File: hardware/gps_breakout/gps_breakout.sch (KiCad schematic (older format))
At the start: 33 parts

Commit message: started layout of gps board
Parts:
- C1, C10, C11, C12, C13, C2, C3, C4, C5, C6, C7, C8, C9: renamed from C?; footprint (none) -> Capacitors_SMD:C_0603
- CON1: renamed from CON?; footprint (none) -> Connect:USB_Mini-B
- D1, D2, D3: renamed from D?; footprint (none) -> LEDs:LED-0603
- L1, L2, L3, L4: renamed from L?; footprint (none) -> Resistors_SMD:R_0603
- P1: renamed from P?; footprint (none) -> sensornode:LPPB061NGCN-RC
- P2: renamed from P?; footprint (none) -> sensornode:CONN_MSPJTAG
- P3, P4, P5: renamed from P?; footprint (none) -> Connect:PINHEAD1-3
- R1, R2, R3, R4: renamed from R?; footprint (none) -> Resistors_SMD:R_0603
- U1: renamed from U?; footprint (none) -> Housings_SOT-89:SOT89-3_Housing
- U2: renamed from U?; footprint (none) -> Housings_SSOP:SSOP-28_5.3x10.2mm_Pitch0.65mm
- U3: renamed from U?; footprint (none) -> sensornode:gps_radionova

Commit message: finished layout of gps board
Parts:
- C5: value 100nF -> 1000nF
- P3, P4, P5: footprint Connect:PINHEAD1-3 -> sensornode:JMP_HDR
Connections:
- net RST is gone; now on net MSP_RST: P2.1 (P1)
- net TCK is gone; now on net MSP_TST: P2.7 (P7)
- net at U3.10 (HRST): now also P5.2 (P2); no longer P5.3 (P3)
- net at U3.11 (1PPS): now also P5.3 (P3); no longer P5.2 (P2)
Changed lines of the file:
@@
 $EndComp
 Text Label 1900 4150 2    60   ~ 0
-TCK
+MSP_TST
 Wire Wire Line
 	2600 3950 2800 3950
@@
 	2100 3850 1900 3850
 Text Label 1900 3850 2    60   ~ 0
-RST
+MSP_RST
 NoConn ~ 2100 3950
 NoConn ~ 2100 4050
@@
 P 4600 6050
 F 0 "C5" H 4610 6120 50  0000 L CNN
-F 1 "100nF" H 4610 5970 50  0000 L CNN
+F 1 "1000nF" H 4610 5970 50  0000 L CNN
 F 2 "Capacitors_SMD:C_0603" H 4600 6050 60  0001 C CNN
 F 3 "" H 4600 6050 60  0000 C CNN
@@
 F 0 "P4" H 4650 2150 50  0000 C CNN
 F 1 "CONN_01X03" V 4750 1950 50  0000 C CNN
-F 2 "Connect:PINHEAD1-3" H 4650 1950 60  0001 C CNN
+F 2 "sensornode:JMP_HDR" H 4650 1950 60  0001 C CNN
 F 3 "" H 4650 1950 60  0000 C CNN
 	1    4650 1950
@@
 F 0 "P3" H 4650 1600 50  0000 C CNN
 F 1 "CONN_01X03" V 4750 1400 50  0000 C CNN
-F 2 "Connect:PINHEAD1-3" H 4650 1400 60  0001 C CNN
+F 2 "sensornode:JMP_HDR" H 4650 1400 60  0001 C CNN
 F 3 "" H 4650 1400 60  0000 C CNN
 	1    4650 1400
@@
 F 0 "P5" H 7150 3300 50  0000 C CNN
 F 1 "CONN_01X03" V 7250 3100 50  0000 C CNN
-F 2 "Connect:PINHEAD1-3" H 7150 3100 60  0001 C CNN
+F 2 "sensornode:JMP_HDR" H 7150 3100 60  0001 C CNN
 F 3 "" H 7150 3100 60  0000 C CNN
 	1    7150 3100
@@
 Wire Wire Line
 	7850 2800 7850 3050
-Wire Wire Line
-	7150 2400 7150 2900
 $Comp
 L GND #PWR032
@@
 Wire Wire Line
 	7150 2300 7050 2300
-Wire Wire Line
-	7050 2300 7050 2900
 $Comp
 L +3V3 #PWR036
@@
 Wire Wire Line
 	6700 3300 6600 3300
+Wire Wire Line
+	7050 2300 7050 2550
+Wire Wire Line
+	7050 2550 7150 2550
+Wire Wire Line
+	7150 2550 7150 2900
+Wire Wire Line
+	7150 2400 7100 2400
+Wire Wire Line
+	7100 2400 7100 2650
+Wire Wire Line
+	7100 2650 7050 2650
+Wire Wire Line
+	7050 2650 7050 2900
 $EndSCHEMATC

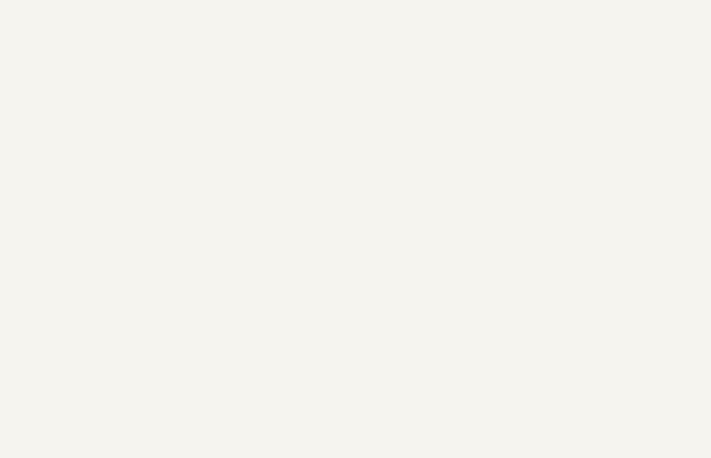
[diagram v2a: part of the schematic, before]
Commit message: ordered gps board
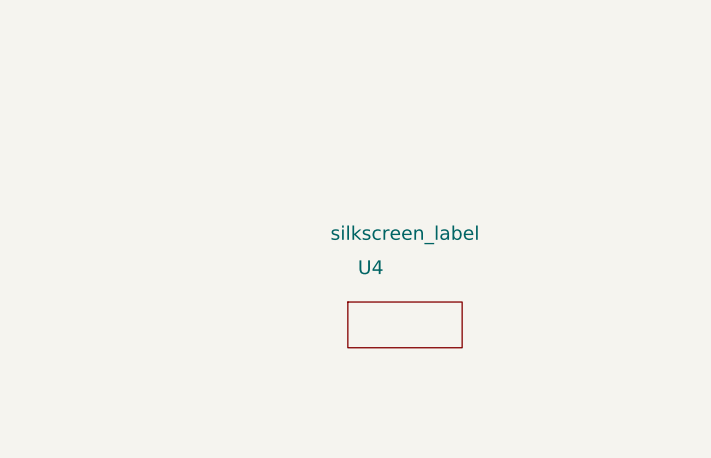
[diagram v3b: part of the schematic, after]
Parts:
- added U4: silkscreen_label, sensornode:gunter, symbol silkscreen_label
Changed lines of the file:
@@
 LIBS:74aup1g157
 LIBS:sn74lvc1g18
+LIBS:silkscreen_label
 LIBS:gps_breakout-cache
 EELAYER 25 0
@@
 Wire Wire Line
 	7050 2650 7050 2900
+$Comp
+L silkscreen_label U4
+U 1 1 562C04C2
+P 9650 6250
+F 0 "U4" H 9450 6450 60  0000 C CNN
+F 1 "silkscreen_label" H 9600 6600 60  0000 C CNN
+F 2 "sensornode:gunter" H 9650 6250 60  0001 C CNN
+F 3 "" H 9650 6250 60  0000 C CNN
+	1    9650 6250
+	1    0    0    -1
+$EndComp
 $EndSCHEMATC

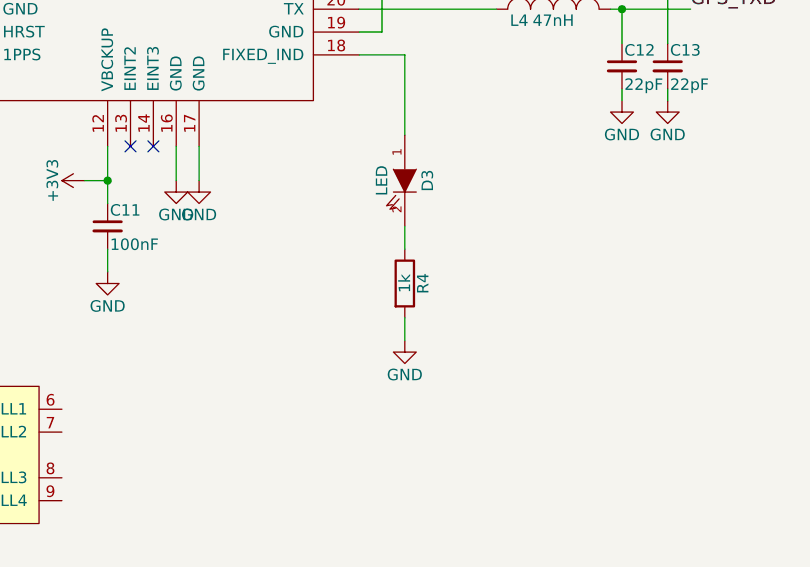
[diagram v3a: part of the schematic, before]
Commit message: added BOM, ordered components
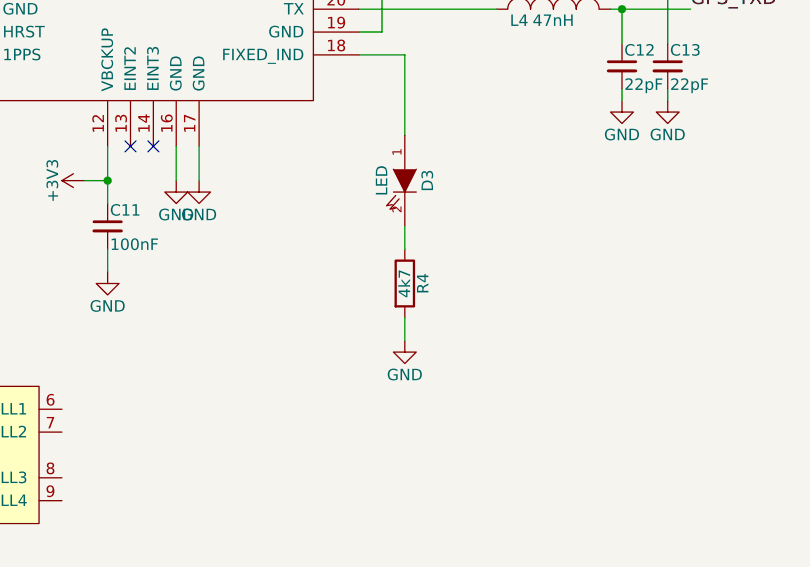
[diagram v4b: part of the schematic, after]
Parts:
- C1, C5, C6: DIST_PN (none) -> 490-1543-1-ND
- C10, C12, C13, C8: DIST_PN (none) -> 490-1411-1-ND
- C11, C2, C3, C4, C7, C9: DIST_PN (none) -> 490-1532-1-ND
- CON1: DIST_PN (none) -> A121533CT-ND
- D1, D2, D3: DIST_PN (none) -> 160-1447-1-ND
- L3, L4: DIST_PN (none) -> 712-1442-1-ND
- P1: DIST_PN (none) -> S9016E-06-ND
- P2: DIST_PN (none) -> S9170-ND
- P3, P4, P5: DIST_PN (none) -> 609-3461-ND
- R1, R2, R3: DIST_PN (none) -> P4.7KGCT-ND
- R4: value 1k -> 4k7; DIST_PN (none) -> P4.7KGCT-ND
- U1: DIST_PN (none) -> MCP1700T3302EMBCT-ND
- U2: DIST_PN (none) -> CY7C65213-28PVXI-ND
- U3: DIST_PN (none) -> 627-1055-1-ND
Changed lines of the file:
@@
 F 2 "Housings_SSOP:SSOP-28_5.3x10.2mm_Pitch0.65mm" H 4650 4150 60  0001 C CNN
 F 3 "" H 4650 4150 60  0000 C CNN
+F 4 "CY7C65213-28PVXI-ND" H 4900 3500 60  0001 C CNN "DIST_PN"
 	1    4900 3500
 	1    0    0    -1
@@
 F 2 "sensornode:gps_radionova" H 7650 2100 60  0001 C CNN
 F 3 "" H 7650 2100 60  0000 C CNN
+F 4 "627-1055-1-ND" H 8050 1900 60  0001 C CNN "DIST_PN"
 	1    8050 1900
 	1    0    0    -1
@@
 F 2 "Connect:USB_Mini-B" H 7150 4050 50  0001 C CNN
 F 3 "" H 7150 4050 50  0000 C CNN
+F 4 "A121533CT-ND" H 7150 4150 60  0001 C CNN "DIST_PN"
 	1    7150 4150
 	1    0    0    -1
@@
 F 2 "Resistors_SMD:R_0603" H 5900 3750 60  0001 C CNN
 F 3 "" H 5900 3750 60  0000 C CNN
+F 4 "P4.7KGCT-ND" H 5900 3750 60  0001 C CNN "DIST_PN"
 	1    5900 3750
 	0    -1   -1   0
@@
 F 2 "sensornode:LPPB061NGCN-RC" H 1700 6400 60  0001 C CNN
 F 3 "" H 1700 6400 60  0000 C CNN
+F 4 "S9016E-06-ND" H 1700 6400 60  0001 C CNN "DIST_PN"
 	1    1700 6400
 	-1   0    0    1
@@
 F 2 "sensornode:CONN_MSPJTAG" H 2350 2950 60  0001 C CNN
 F 3 "" H 2350 2950 60  0000 C CNN
+F 4 "S9170-ND" H 2350 4150 60  0001 C CNN "DIST_PN"
 	1    2350 4150
 	1    0    0    -1
@@
 F 2 "Capacitors_SMD:C_0603" H 4250 6050 60  0001 C CNN
 F 3 "" H 4250 6050 60  0000 C CNN
+F 4 "490-1532-1-ND" H 4250 6050 60  0001 C CNN "DIST_PN"
 	1    4250 6050
 	1    0    0    -1
@@
 F 2 "Capacitors_SMD:C_0603" H 4600 6050 60  0001 C CNN
 F 3 "" H 4600 6050 60  0000 C CNN
+F 4 "490-1543-1-ND" H 4600 6050 60  0001 C CNN "DIST_PN"
 	1    4600 6050
 	1    0    0    -1
@@
 F 2 "Capacitors_SMD:C_0603" H 6300 3750 60  0001 C CNN
 F 3 "" H 6300 3750 60  0000 C CNN
+F 4 "490-1532-1-ND" H 6300 3750 60  0001 C CNN "DIST_PN"
 	1    6300 3750
 	1    0    0    -1
@@
 F 2 "Housings_SOT-89:SOT89-3_Housing" H 2700 2000 60  0001 C CNN
 F 3 "" H 2700 2000 60  0000 C CNN
+F 4 "MCP1700T3302EMBCT-ND" H 2650 2000 60  0001 C CNN "DIST_PN"
 	1    2650 2000
 	1    0    0    -1
@@
 F 2 "Capacitors_SMD:C_0603" H 1950 2350 60  0001 C CNN
 F 3 "" H 1950 2350 60  0000 C CNN
+F 4 "490-1532-1-ND" H 1950 2350 60  0001 C CNN "DIST_PN"
 	1    1950 2350
 	1    0    0    -1
@@
 F 2 "Capacitors_SMD:C_0603" H 1500 2350 60  0001 C CNN
 F 3 "" H 1500 2350 60  0000 C CNN
+F 4 "490-1543-1-ND" H 1500 2350 60  0001 C CNN "DIST_PN"
 	1    1500 2350
 	1    0    0    -1
@@
 F 2 "Capacitors_SMD:C_0603" H 2350 1400 60  0001 C CNN
 F 3 "" H 2350 1400 60  0000 C CNN
+F 4 "490-1532-1-ND" H 2350 1400 60  0001 C CNN "DIST_PN"
 	1    2350 1400
 	1    0    0    -1
@@
 F 2 "sensornode:JMP_HDR" H 4650 1950 60  0001 C CNN
 F 3 "" H 4650 1950 60  0000 C CNN
+F 4 "609-3461-ND" H 4650 1950 60  0001 C CNN "DIST_PN"
 	1    4650 1950
 	1    0    0    -1
@@
 F 2 "sensornode:JMP_HDR" H 4650 1400 60  0001 C CNN
 F 3 "" H 4650 1400 60  0000 C CNN
+F 4 "609-3461-ND" H 4650 1400 60  0001 C CNN "DIST_PN"
 	1    4650 1400
 	1    0    0    -1
@@
 F 2 "Resistors_SMD:R_0603" H 9800 2100 60  0001 C CNN
 F 3 "" H 9800 2100 60  0000 C CNN
+F 4 "712-1442-1-ND" H 9800 2100 60  0001 C CNN "DIST_PN"
 	1    9800 2100
 	1    0    0    -1
@@
 F 2 "Resistors_SMD:R_0603" H 9800 2200 60  0001 C CNN
 F 3 "" H 9800 2200 60  0000 C CNN
+F 4 "712-1442-1-ND" H 9800 2200 60  0001 C CNN "DIST_PN"
 	1    9800 2200
 	1    0    0    -1
@@
 F 2 "Capacitors_SMD:C_0603" H 10100 2450 60  0001 C CNN
 F 3 "" H 10100 2450 60  0000 C CNN
+F 4 "490-1411-1-ND" H 10100 2450 60  0001 C CNN "DIST_PN"
 	1    10100 2450
 	1    0    0    -1
@@
 F 2 "Capacitors_SMD:C_0603" H 10300 2450 60  0001 C CNN
 F 3 "" H 10300 2450 60  0000 C CNN
+F 4 "490-1411-1-ND" H 10300 2450 60  0001 C CNN "DIST_PN"
 	1    10300 2450
 	1    0    0    -1
@@
 F 2 "Capacitors_SMD:C_0603" H 6400 1800 60  0001 C CNN
 F 3 "" H 6400 1800 60  0000 C CNN
+F 4 "490-1411-1-ND" H 6400 1800 60  0001 C CNN "DIST_PN"
 	1    6400 1800
 	1    0    0    -1
@@
 F 2 "Capacitors_SMD:C_0603" H 6450 2300 60  0001 C CNN
 F 3 "" H 6450 2300 60  0000 C CNN
+F 4 "490-1532-1-ND" H 6450 2300 60  0001 C CNN "DIST_PN"
 	1    6450 2300
 	1    0    0    -1
@@
 F 2 "sensornode:JMP_HDR" H 7150 3100 60  0001 C CNN
 F 3 "" H 7150 3100 60  0000 C CNN
+F 4 "609-3461-ND" H 7150 3100 60  0001 C CNN "DIST_PN"
 	1    7150 3100
 	0    1    1    0
@@
 F 2 "LEDs:LED-0603" H 9150 2950 60  0001 C CNN
 F 3 "" H 9150 2950 60  0000 C CNN
+F 4 "160-1447-1-ND" H 9150 2950 60  0001 C CNN "DIST_PN"
 	1    9150 2950
 	0    1    1    0
@@
 P 9150 3400
 F 0 "R4" V 9230 3400 50  0000 C CNN
-F 1 "1k" V 9150 3400 50  0000 C CNN
+F 1 "4k7" V 9150 3400 50  0000 C CNN
 F 2 "Resistors_SMD:R_0603" V 9080 3400 30  0001 C CNN
 F 3 "" H 9150 3400 30  0000 C CNN
+F 4 "P4.7KGCT-ND" H 9150 3400 60  0001 C CNN "DIST_PN"
 	1    9150 3400
 	1    0    0    -1
@@
 F 2 "Capacitors_SMD:C_0603" H 6700 2300 60  0001 C CNN
 F 3 "" H 6700 2300 60  0000 C CNN
+F 4 "490-1411-1-ND" H 6700 2300 60  0001 C CNN "DIST_PN"
 	1    6700 2300
 	1    0    0    -1
@@
 F 2 "Capacitors_SMD:C_0603" H 7850 3150 60  0001 C CNN
 F 3 "" H 7850 3150 60  0000 C CNN
+F 4 "490-1532-1-ND" H 7850 3150 60  0001 C CNN "DIST_PN"
 	1    7850 3150
 	1    0    0    -1
@@
 F 2 "Capacitors_SMD:C_0603" H 5750 4400 60  0001 C CNN
 F 3 "" H 5750 4400 60  0000 C CNN
+F 4 "490-1543-1-ND" H 5750 4400 60  0001 C CNN "DIST_PN"
 	1    5750 4400
 	1    0    0    -1
@@
 F 2 "LEDs:LED-0603" H 6400 3100 60  0001 C CNN
 F 3 "" H 6400 3100 60  0000 C CNN
+F 4 "160-1447-1-ND" H 6400 3100 60  0001 C CNN "DIST_PN"
 	1    6400 3100
 	-1   0    0    1
@@
 F 2 "Resistors_SMD:R_0603" H 6000 3100 60  0001 C CNN
 F 3 "" H 6000 3100 60  0000 C CNN
+F 4 "P4.7KGCT-ND" H 6000 3100 60  0001 C CNN "DIST_PN"
 	1    6000 3100
 	0    -1   -1   0
@@
 F 2 "LEDs:LED-0603" H 6400 3300 60  0001 C CNN
 F 3 "" H 6400 3300 60  0000 C CNN
+F 4 "160-1447-1-ND" H 6400 3300 60  0001 C CNN "DIST_PN"
 	1    6400 3300
 	-1   0    0    1
@@
 F 2 "Resistors_SMD:R_0603" H 6000 3300 60  0001 C CNN
 F 3 "" H 6000 3300 60  0000 C CNN
+F 4 "P4.7KGCT-ND" H 6000 3300 60  0001 C CNN "DIST_PN"
 	1    6000 3300
 	0    -1   -1   0
